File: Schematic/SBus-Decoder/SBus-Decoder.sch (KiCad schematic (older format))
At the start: 12 parts, among them J1 Conn_01x03_Male, J2 Conn_01x03_Male, J3 Conn_01x02_Male, J4 Conn_01x03_Male, J5 Conn_01x03_Male, U1 MCP1703A-3302_SOT223, U2 PIC16F18313-I_SN

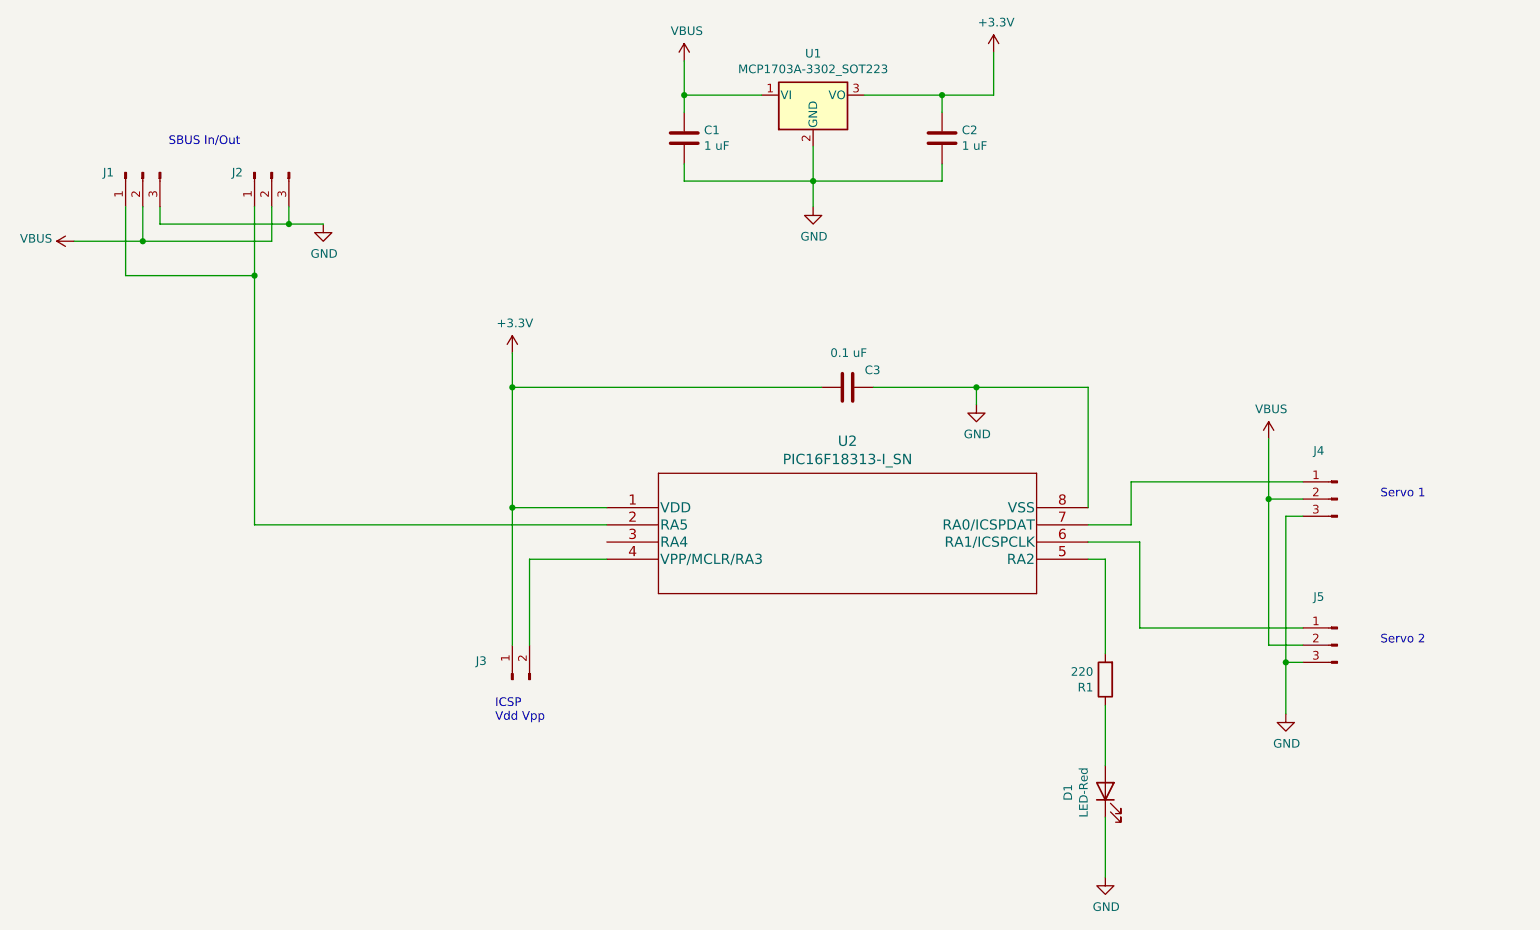
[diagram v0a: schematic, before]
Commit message: Added CLC connections
Need CLC to invert SBus serial signal
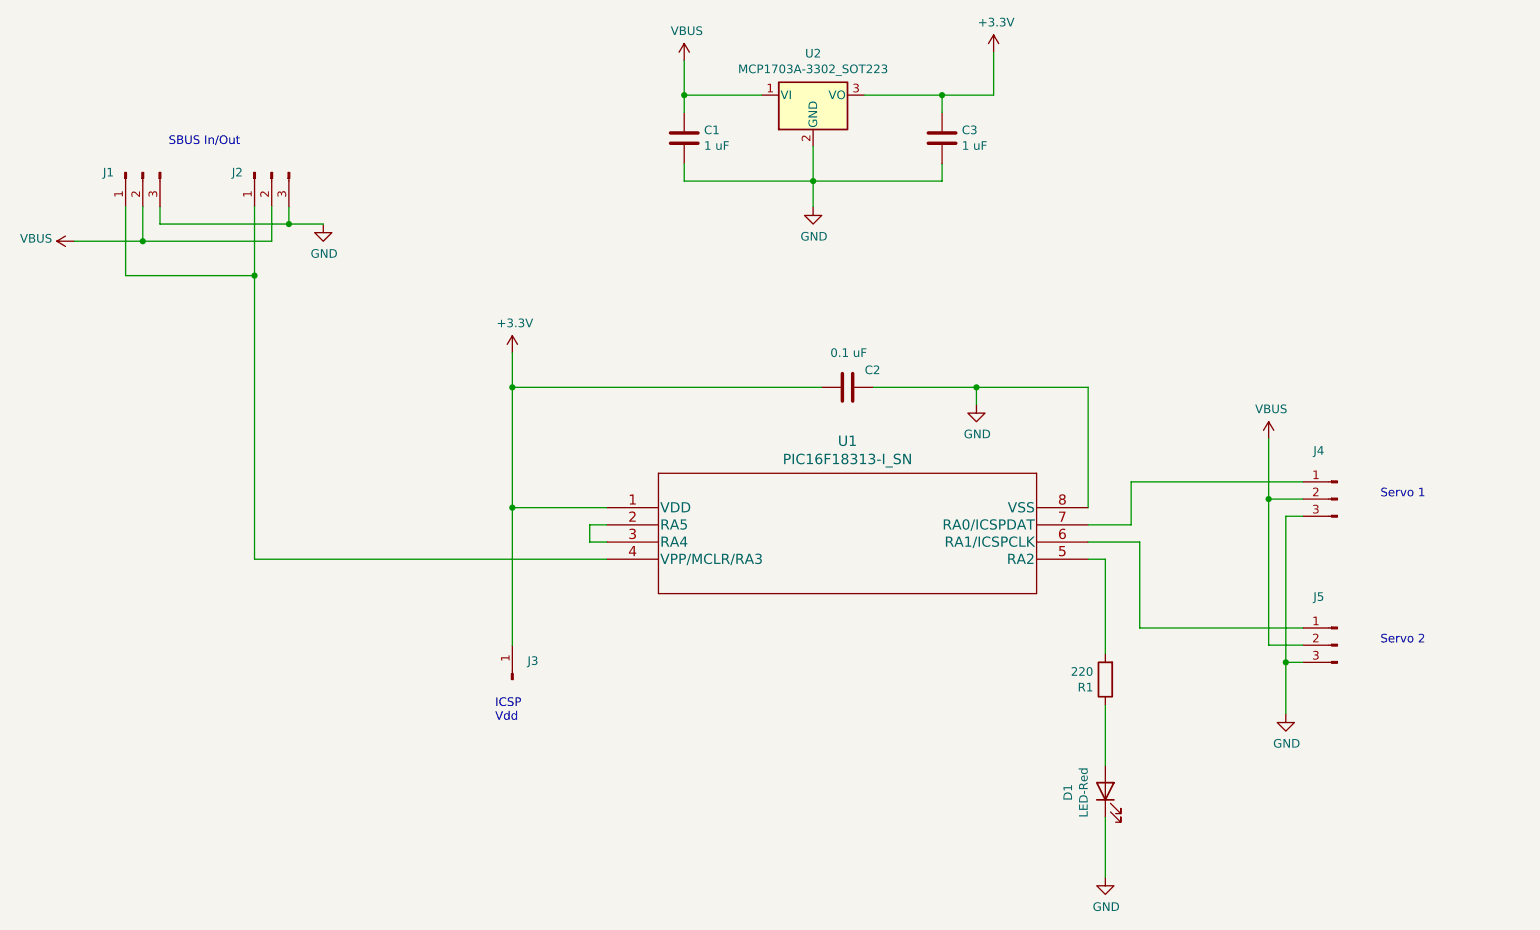
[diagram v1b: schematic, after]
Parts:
- removed J3: Conn_01x02_Male, Connector_PinHeader_2.54mm:PinHeader_1x02_P2.54mm_Vertical, symbol Connector:Conn_01x02_Male
- added J3: Conn_01x01_Male, Connector_PinHeader_2.54mm:PinHeader_1x01_P2.54mm_Vertical, symbol Connector:Conn_01x01_Male
- renumbered C3 to C2, C2 to C3, U2 to U1, U1 to U2
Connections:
- net +3V3: now also J3.1 (Pin_1)
- net at J1.1 (Pin_1), J2.1 (Pin_1): now also U1.4 (VPP/MCLR/RA3); no longer U1.2 (RA5)
- net at U1.3 (RA4): now also U1.2 (RA5)
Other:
- note added: "ICSP \nVdd"
- note removed: "ICSP \nVdd Vpp"
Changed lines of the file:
@@
 $EndDescr
 $Comp
-L PIC16F18313:PIC16F18313-I_SN U2
+L PIC16F18313:PIC16F18313-I_SN U1
 U 1 1 60EFBC4A
 P 4000 3650
-F 0 "U2" H 5400 4037 60  0000 C CNN
+F 0 "U1" H 5400 4037 60  0000 C CNN
 F 1 "PIC16F18313-I_SN" H 5400 3931 60  0000 C CNN
 F 2 "SOIC8_SN_MCH" H 5400 3890 60  0001 C CNN
@@
 $EndComp
 $Comp
-L power:GND #PWR07
+L power:GND #PWR010
 U 1 1 60F15387
 P 7950 4850
-F 0 "#PWR07" H 7950 4600 50  0001 C CNN
+F 0 "#PWR010" H 7950 4600 50  0001 C CNN
 F 1 "GND" H 7955 4677 50  0000 C CNN
 F 2 "" H 7950 4850 50  0001 C CNN
@@
 $EndComp
 $Comp
-L Regulator_Linear:MCP1703A-3302_SOT223 U1
+L Regulator_Linear:MCP1703A-3302_SOT223 U2
 U 1 1 60F273AB
 P 5200 1250
-F 0 "U1" H 5200 1492 50  0000 C CNN
+F 0 "U2" H 5200 1492 50  0000 C CNN
 F 1 "MCP1703A-3302_SOT223" H 5200 1401 50  0000 C CNN
 F 2 "Package_TO_SOT_SMD:SOT-223-3_TabPin2" H 5200 1450 50  0001 C CNN
@@
 $EndComp
 $Comp
-L Device:C C2
+L Device:C C3
 U 1 1 60F28E0E
 P 5950 1500
-F 0 "C2" H 6065 1546 50  0000 L CNN
+F 0 "C3" H 6065 1546 50  0000 L CNN
 F 1 "1 uF" H 6065 1455 50  0000 L CNN
 F 2 "Capacitor_SMD:C_0603_1608Metric" H 5988 1350 50  0001 C CNN
@@
 $EndComp
 $Comp
-L Device:C C3
+L Device:C C2
 U 1 1 60F28F04
 P 5400 2950
-F 0 "C3" V 5300 3050 50  0000 L CNN
+F 0 "C2" V 5300 3050 50  0000 L CNN
 F 1 "0.1 uF" V 5200 2850 50  0000 L CNN
 F 2 "Capacitor_SMD:C_0603_1608Metric" H 5438 2800 50  0001 C CNN
@@
 $EndComp
 $Comp
-L power:GND #PWR04
+L power:GND #PWR06
 U 1 1 60F291DB
 P 6150 3050
-F 0 "#PWR04" H 6150 2800 50  0001 C CNN
+F 0 "#PWR06" H 6150 2800 50  0001 C CNN
 F 1 "GND" H 6155 2877 50  0000 C CNN
 F 2 "" H 6150 3050 50  0001 C CNN
@@
 	1    6150 3050
 	1    0    0    -1
-$EndComp
-$Comp
-L Connector:Conn_01x02_Male J3
-U 1 1 60F29653
-P 3450 4650
-F 0 "J3" V 3558 4831 50  0000 C CNN
-F 1 "Conn_01x02_Male" H 3558 4740 50  0001 C CNN
-F 2 "Connector_PinHeader_2.54mm:PinHeader_1x02_P2.54mm_Vertical" H 3450 4650 50  0001 C CNN
-F 3 "~" H 3450 4650 50  0001 C CNN
-	1    3450 4650
-	0    -1   -1   0
 $EndComp
 $Comp
@@
 Servo 2
 Text Notes 3350 4900 0    50   ~ 0
-ICSP \nVdd Vpp
+ICSP \nVdd
 Wire Wire Line
 	4000 3650 3450 3650
 Wire Wire Line
 	3450 3650 3450 4450
-Wire Wire Line
-	4000 3950 3550 3950
-Wire Wire Line
-	3550 3950 3550 4450
 Wire Wire Line
 	5550 2950 6150 2950
@@
 	4450 1250 4450 1350
 $Comp
-L power:GND #PWR03
+L power:GND #PWR05
 U 1 1 60F2B5D7
 P 5200 1900
-F 0 "#PWR03" H 5200 1650 50  0001 C CNN
+F 0 "#PWR05" H 5200 1650 50  0001 C CNN
 F 1 "GND" H 5205 1727 50  0000 C CNN
 F 2 "" H 5200 1900 50  0001 C CNN
@@
 	7950 4550 7950 4850
 $Comp
-L power:VBUS #PWR06
+L power:VBUS #PWR09
 U 1 1 60F32EF0
 P 7850 3250
-F 0 "#PWR06" H 7850 3100 50  0001 C CNN
+F 0 "#PWR09" H 7850 3100 50  0001 C CNN
 F 1 "VBUS" H 7865 3423 50  0000 C CNN
 F 2 "" H 7850 3250 50  0001 C CNN
@@
 	2150 2000 2350 2000
 Connection ~ 2150 2000
-Wire Wire Line
-	4000 3750 1950 3750
-Wire Wire Line
-	1950 3750 1950 2300
 Connection ~ 1950 2300
 $Comp
-L power:GND #PWR05
+L power:GND #PWR08
 U 1 1 60F3C16F
 P 6900 5800
-F 0 "#PWR05" H 6900 5550 50  0001 C CNN
+F 0 "#PWR08" H 6900 5550 50  0001 C CNN
 F 1 "GND" H 6905 5627 50  0000 C CNN
 F 2 "" H 6900 5800 50  0001 C CNN
@@
 	6900 5450 6900 5800
 $Comp
-L power:VBUS #PWR?
+L power:VBUS #PWR04
 U 1 1 60F3F9A0
 P 4450 1050
-F 0 "#PWR?" H 4450 900 50  0001 C CNN
+F 0 "#PWR04" H 4450 900 50  0001 C CNN
 F 1 "VBUS" H 4465 1223 50  0000 C CNN
 F 2 "" H 4450 1050 50  0001 C CNN
@@
 	3450 2950 5250 2950
 $Comp
-L power:+3.3V #PWR?
+L power:+3.3V #PWR07
 U 1 1 60F41144
 P 6250 1000
-F 0 "#PWR?" H 6250 850 50  0001 C CNN
+F 0 "#PWR07" H 6250 850 50  0001 C CNN
 F 1 "+3.3V" H 6265 1173 50  0000 C CNN
 F 2 "" H 6250 1000 50  0001 C CNN
@@
 $EndComp
 $Comp
-L power:+3.3V #PWR?
+L power:+3.3V #PWR03
 U 1 1 60F41B17
 P 3450 2750
-F 0 "#PWR?" H 3450 2600 50  0001 C CNN
+F 0 "#PWR03" H 3450 2600 50  0001 C CNN
 F 1 "+3.3V" H 3465 2923 50  0000 C CNN
 F 2 "" H 3450 2750 50  0001 C CNN
@@
 Wire Wire Line
 	6250 1000 6250 1250
+Wire Wire Line
+	1950 2300 1950 3950
+Wire Wire Line
+	4000 3850 3900 3850
+Wire Wire Line
+	3900 3850 3900 3750
+Wire Wire Line
+	3900 3750 4000 3750
+Wire Wire Line
+	1950 3950 4000 3950
+$Comp
+L Connector:Conn_01x01_Male J3
+U 1 1 60F2444D
+P 3450 4650
+F 0 "J3" V 3558 4562 50  0000 R CNN
+F 1 "Conn_01x01_Male" V 3513 4562 50  0001 R CNN
+F 2 "Connector_PinHeader_2.54mm:PinHeader_1x01_P2.54mm_Vertical" H 3450 4650 50  0001 C CNN
+F 3 "~" H 3450 4650 50  0001 C CNN
+	1    3450 4650
+	0    -1   -1   0
+$EndComp
 $EndSCHEMATC

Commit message: Changed connectors
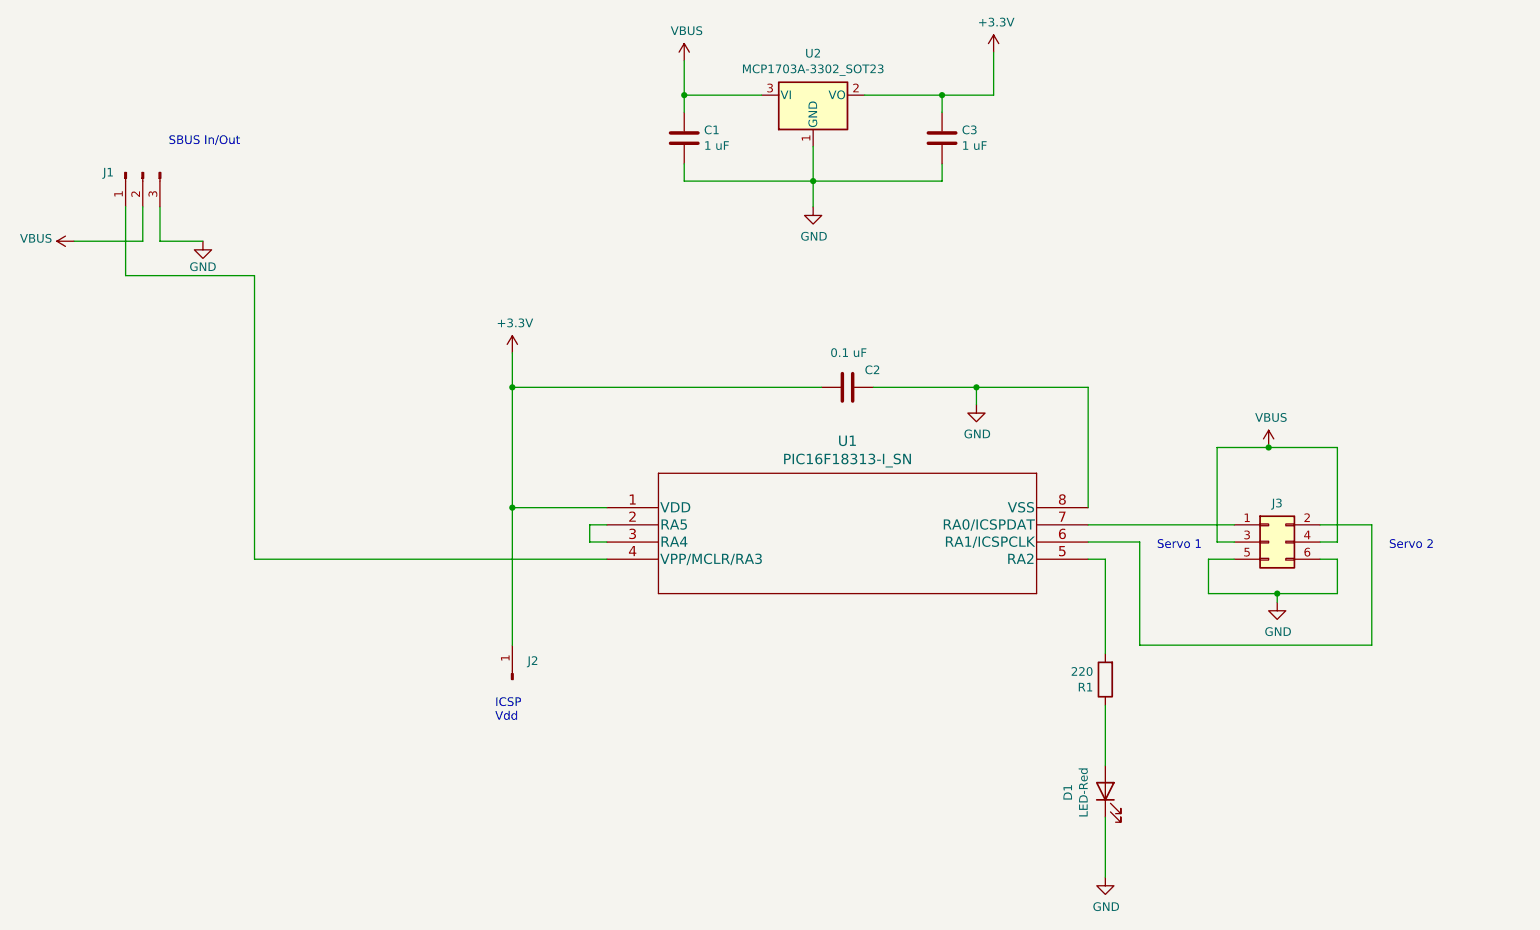
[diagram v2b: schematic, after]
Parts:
- removed J2, J4, J5: Conn_01x03_Male, Connector_PinHeader_2.54mm:PinHeader_1x03_P2.54mm_Horizontal, symbol Connector:Conn_01x03_Male
- removed U2: MCP1703A-3302_SOT223, Package_TO_SOT_SMD:SOT-223-3_TabPin2, symbol Regulator_Linear:MCP1703A-3302_SOT223
- added J3: Conn_02x03_Odd_Even, Connector_PinHeader_2.54mm:PinHeader_2x03_P2.54mm_Horizontal, symbol Connector_Generic:Conn_02x03_Odd_Even
- added U2: MCP1703A-3302_SOT23, Package_TO_SOT_SMD:SOT-23, symbol Regulator_Linear:MCP1703A-3302_SOT23
- J1: footprint Connector_PinHeader_2.54mm:PinHeader_1x03_P2.54mm_Horizontal -> Connector_Wire:SolderWire-0.75sqmm_1x03_P4.8mm_D1.25mm_OD2.3mm
- U1: footprint SOIC8_SN_MCH -> PIC16F18313:PIC16F18313-I&slash_SN
- renumbered J3 to J2
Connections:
- net +3V3: now also U2.2 (VO)
- net GND: now also J3.5 (Pin_5), J3.6 (Pin_6), U2.1 (GND)
- net VBUS: now also J3.3 (Pin_3), J3.4 (Pin_4), U2.3 (VI)
- net at U1.6 (RA1/ICSPCLK): now also J3.2 (Pin_2)
- net at U1.7 (RA0/ICSPDAT): now also J3.1 (Pin_1)
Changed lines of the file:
@@
 F 0 "U1" H 5400 4037 60  0000 C CNN
 F 1 "PIC16F18313-I_SN" H 5400 3931 60  0000 C CNN
-F 2 "SOIC8_SN_MCH" H 5400 3890 60  0001 C CNN
+F 2 "PIC16F18313:PIC16F18313-I&slash_SN" H 5400 3890 60  0001 C CNN
 F 3 "" H 4000 3650 60  0000 C CNN
 	1    4000 3650
 	1    0    0    -1
-$EndComp
-$Comp
-L Connector:Conn_01x03_Male J4
-U 1 1 60F0F917
-P 8250 3600
-F 0 "J4" H 8358 3881 50  0000 C CNN
-F 1 "Conn_01x03_Male" H 8358 3790 50  0001 C CNN
-F 2 "Connector_PinHeader_2.54mm:PinHeader_1x03_P2.54mm_Horizontal" H 8250 3600 50  0001 C CNN
-F 3 "~" H 8250 3600 50  0001 C CNN
-	1    8250 3600
-	-1   0    0    -1
 $EndComp
 $Comp
@@
 L power:GND #PWR010
 U 1 1 60F15387
-P 7950 4850
-F 0 "#PWR010" H 7950 4600 50  0001 C CNN
-F 1 "GND" H 7955 4677 50  0000 C CNN
-F 2 "" H 7950 4850 50  0001 C CNN
-F 3 "" H 7950 4850 50  0001 C CNN
-	1    7950 4850
-	1    0    0    -1
-$EndComp
-$Comp
-L Connector:Conn_01x03_Male J2
-U 1 1 60F26177
-P 2050 1700
-F 0 "J2" V 2050 1900 50  0000 C CNN
-F 1 "Conn_01x03_Male" H 2158 1890 50  0001 C CNN
-F 2 "Connector_PinHeader_2.54mm:PinHeader_1x03_P2.54mm_Horizontal" H 2050 1700 50  0001 C CNN
-F 3 "~" H 2050 1700 50  0001 C CNN
-	1    2050 1700
-	0    -1   1    0
-$EndComp
-$Comp
-L Connector:Conn_01x03_Male J5
-U 1 1 60F264CF
-P 8250 4450
-F 0 "J5" H 8358 4731 50  0000 C CNN
-F 1 "Conn_01x03_Male" H 8358 4640 50  0001 C CNN
-F 2 "Connector_PinHeader_2.54mm:PinHeader_1x03_P2.54mm_Horizontal" H 8250 4450 50  0001 C CNN
-F 3 "~" H 8250 4450 50  0001 C CNN
-	1    8250 4450
-	-1   0    0    -1
-$EndComp
-$Comp
-L Regulator_Linear:MCP1703A-3302_SOT223 U2
-U 1 1 60F273AB
-P 5200 1250
-F 0 "U2" H 5200 1492 50  0000 C CNN
-F 1 "MCP1703A-3302_SOT223" H 5200 1401 50  0000 C CNN
-F 2 "Package_TO_SOT_SMD:SOT-223-3_TabPin2" H 5200 1450 50  0001 C CNN
-F 3 "http://ww1.microchip.com/downloads/en/DeviceDoc/20005122B.pdf" H 5200 1200 50  0001 C CNN
-	1    5200 1250
+P 7900 4200
+F 0 "#PWR010" H 7900 3950 50  0001 C CNN
+F 1 "GND" H 7905 4027 50  0000 C CNN
+F 2 "" H 7900 4200 50  0001 C CNN
+F 3 "" H 7900 4200 50  0001 C CNN
+	1    7900 4200
 	1    0    0    -1
 $EndComp
@@
 F 0 "J1" V 1300 1900 50  0000 C CNN
 F 1 "Conn_01x03_Male" H 1408 1890 50  0001 C CNN
-F 2 "Connector_PinHeader_2.54mm:PinHeader_1x03_P2.54mm_Horizontal" H 1300 1700 50  0001 C CNN
+F 2 "Connector_Wire:SolderWire-0.75sqmm_1x03_P4.8mm_D1.25mm_OD2.3mm" H 1300 1700 50  0001 C CNN
 F 3 "~" H 1300 1700 50  0001 C CNN
 	1    1300 1700
@@
 Text Notes 1450 1550 0    50   ~ 0
 SBUS In/Out
-Text Notes 8500 3600 0    50   ~ 0
+Text Notes 7200 3900 0    50   ~ 0
 Servo 1
-Text Notes 8500 4450 0    50   ~ 0
+Text Notes 8550 3900 0    50   ~ 0
 Servo 2
 Text Notes 3350 4900 0    50   ~ 0
@@
 	5950 1750 5200 1750
 Wire Wire Line
-	6800 3750 7050 3750
-Wire Wire Line
-	7050 3750 7050 3500
-Wire Wire Line
-	7050 3500 8050 3500
-Wire Wire Line
 	6800 3850 7100 3850
-Wire Wire Line
-	7100 3850 7100 4350
-Wire Wire Line
-	7100 4350 8050 4350
-Wire Wire Line
-	8050 4450 7850 4450
-Wire Wire Line
-	7850 4450 7850 3600
-Wire Wire Line
-	7850 3600 8050 3600
-Wire Wire Line
-	8050 3700 7950 3700
-Wire Wire Line
-	7950 3700 7950 4550
-Wire Wire Line
-	8050 4550 7950 4550
-Connection ~ 7950 4550
-Wire Wire Line
-	7950 4550 7950 4850
 $Comp
 L power:VBUS #PWR09
 U 1 1 60F32EF0
-P 7850 3250
-F 0 "#PWR09" H 7850 3100 50  0001 C CNN
-F 1 "VBUS" H 7865 3423 50  0000 C CNN
-F 2 "" H 7850 3250 50  0001 C CNN
-F 3 "" H 7850 3250 50  0001 C CNN
-	1    7850 3250
-	1    0    0    -1
-$EndComp
-Wire Wire Line
-	7850 3600 7850 3250
-Connection ~ 7850 3600
+P 7850 3300
+F 0 "#PWR09" H 7850 3150 50  0001 C CNN
+F 1 "VBUS" H 7865 3473 50  0000 C CNN
+F 2 "" H 7850 3300 50  0001 C CNN
+F 3 "" H 7850 3300 50  0001 C CNN
+	1    7850 3300
+	1    0    0    -1
+$EndComp
 $Comp
 L power:VBUS #PWR01
@@
 	1300 2100 1300 1900
 Wire Wire Line
-	2050 1900 2050 2100
-Wire Wire Line
-	2050 2100 1300 2100
-Connection ~ 1300 2100
-Wire Wire Line
 	1200 1900 1200 2300
 Wire Wire Line
 	1200 2300 1950 2300
-Wire Wire Line
-	1950 2300 1950 1900
-Wire Wire Line
-	1400 1900 1400 2000
-Wire Wire Line
-	1400 2000 2150 2000
-Wire Wire Line
-	2150 2000 2150 1900
-$Comp
-L power:GND #PWR02
-U 1 1 60F37DA9
-P 2350 2000
-F 0 "#PWR02" H 2350 1750 50  0001 C CNN
-F 1 "GND" H 2355 1827 50  0000 C CNN
-F 2 "" H 2350 2000 50  0001 C CNN
-F 3 "" H 2350 2000 50  0001 C CNN
-	1    2350 2000
-	1    0    0    -1
-$EndComp
-Wire Wire Line
-	2150 2000 2350 2000
-Connection ~ 2150 2000
-Connection ~ 1950 2300
 $Comp
 L power:GND #PWR08
@@
 	1950 3950 4000 3950
 $Comp
-L Connector:Conn_01x01_Male J3
+L Connector:Conn_01x01_Male J2
 U 1 1 60F2444D
 P 3450 4650
-F 0 "J3" V 3558 4562 50  0000 R CNN
+F 0 "J2" V 3558 4562 50  0000 R CNN
 F 1 "Conn_01x01_Male" V 3513 4562 50  0001 R CNN
 F 2 "Connector_PinHeader_2.54mm:PinHeader_1x01_P2.54mm_Vertical" H 3450 4650 50  0001 C CNN
@@
 	0    -1   -1   0
 $EndComp
+$Comp
+L Regulator_Linear:MCP1703A-3302_SOT23 U2
+U 1 1 60F50A9F
+P 5200 1250
+F 0 "U2" H 5200 1492 50  0000 C CNN
+F 1 "MCP1703A-3302_SOT23" H 5200 1401 50  0000 C CNN
+F 2 "Package_TO_SOT_SMD:SOT-23" H 5200 1450 50  0001 C CNN
+F 3 "http://ww1.microchip.com/downloads/en/DeviceDoc/20005122B.pdf" H 5200 1200 50  0001 C CNN
+	1    5200 1250
+	1    0    0    -1
+$EndComp
+$Comp
+L power:GND #PWR02
+U 1 1 60F5D84A
+P 1650 2100
+F 0 "#PWR02" H 1650 1850 50  0001 C CNN
+F 1 "GND" H 1650 1950 50  0000 C CNN
+F 2 "" H 1650 2100 50  0001 C CNN
+F 3 "" H 1650 2100 50  0001 C CNN
+	1    1650 2100
+	1    0    0    -1
+$EndComp
+Wire Wire Line
+	1400 2100 1650 2100
+Wire Wire Line
+	1400 1900 1400 2100
+Wire Wire Line
+	8150 3950 8250 3950
+Wire Wire Line
+	8250 3950 8250 4150
+Wire Wire Line
+	8250 4150 7900 4150
+Wire Wire Line
+	7900 4150 7900 4200
+Wire Wire Line
+	7650 3950 7500 3950
+Wire Wire Line
+	7500 3950 7500 4150
+Connection ~ 7900 4150
+Wire Wire Line
+	7100 4450 8450 4450
+Wire Wire Line
+	8450 3750 8150 3750
+Wire Wire Line
+	7500 4150 7900 4150
+Wire Wire Line
+	8450 3750 8450 4450
+Wire Wire Line
+	8150 3850 8250 3850
+Wire Wire Line
+	8250 3850 8250 3300
+Wire Wire Line
+	8250 3300 7850 3300
+Wire Wire Line
+	7650 3850 7550 3850
+Wire Wire Line
+	7550 3850 7550 3300
+Wire Wire Line
+	7550 3300 7850 3300
+Connection ~ 7850 3300
+Wire Wire Line
+	7100 3850 7100 4450
+Wire Wire Line
+	6800 3750 7650 3750
+$Comp
+L Connector_Generic:Conn_02x03_Odd_Even J3
+U 1 1 60F76AF8
+P 7850 3850
+F 0 "J3" H 7900 4075 50  0000 C CNN
+F 1 "Conn_02x03_Odd_Even" H 7900 4076 50  0001 C CNN
+F 2 "Connector_PinHeader_2.54mm:PinHeader_2x03_P2.54mm_Horizontal" H 7850 3850 50  0001 C CNN
+F 3 "~" H 7850 3850 50  0001 C CNN
+	1    7850 3850
+	1    0    0    -1
+$EndComp
 $EndSCHEMATC
